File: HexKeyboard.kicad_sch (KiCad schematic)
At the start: 82 parts, among them J1 Conn_02x04_Odd_Even, J2 Conn_01x04, J4 USB_A, J9 Micro_SD_Card, SW1 SW_1, SW10 SW_10, SW11 SW_11, SW12 SW_12, SW13 SW_13, SW14 SW_14, SW15 SW_15, SW16 SW_16, SW17 SW_17, SW18 SW_18, SW19 SW_19, SW2 SW_2, SW20 SW_20, SW21 SW_21, SW22 SW_22, SW23 SW_23, SW24 SW_24, SW25 SW_25, SW3 SW_3, SW4 SW_4, SW5 SW_5, SW6 SW_6, SW7 SW_7, SW8 SW_8, SW9 SW_9, U1 ATmega32U4-AU, U2 AMS1117-3.3, U3 74LVC125, U4 AT24CS64-XHM, U5 MAX7219, Y1 16MHz

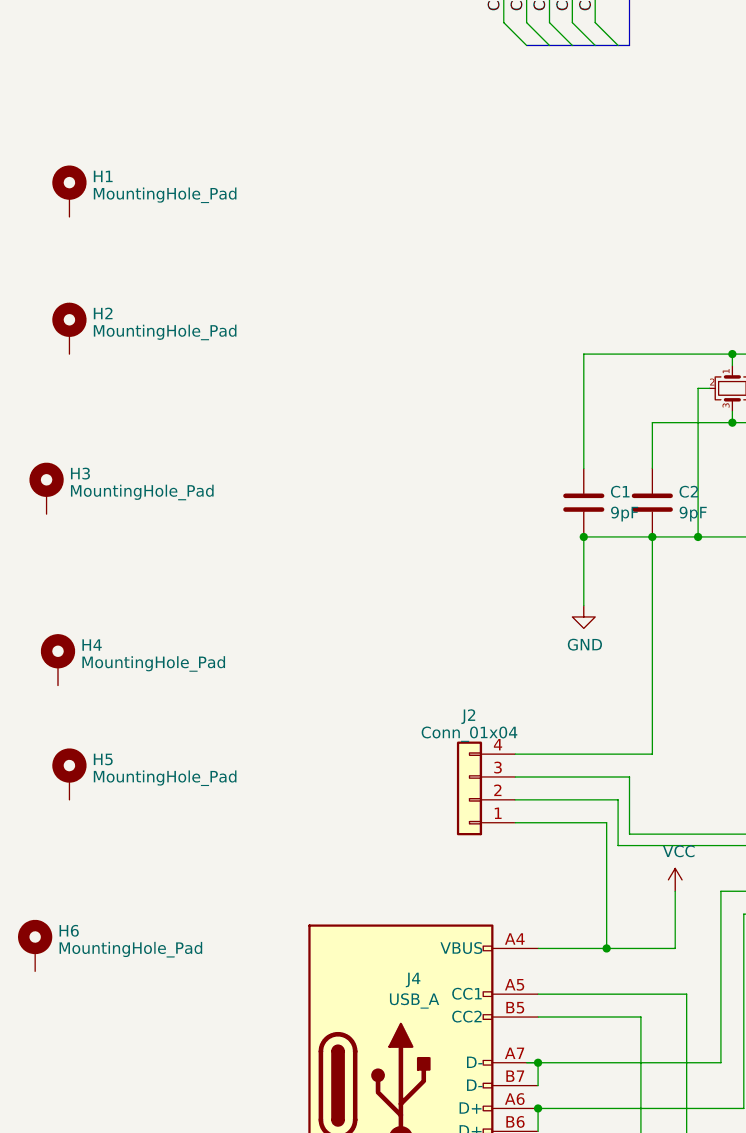
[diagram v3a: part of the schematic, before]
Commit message: Connected mounting holes to Gnd Added filled zone
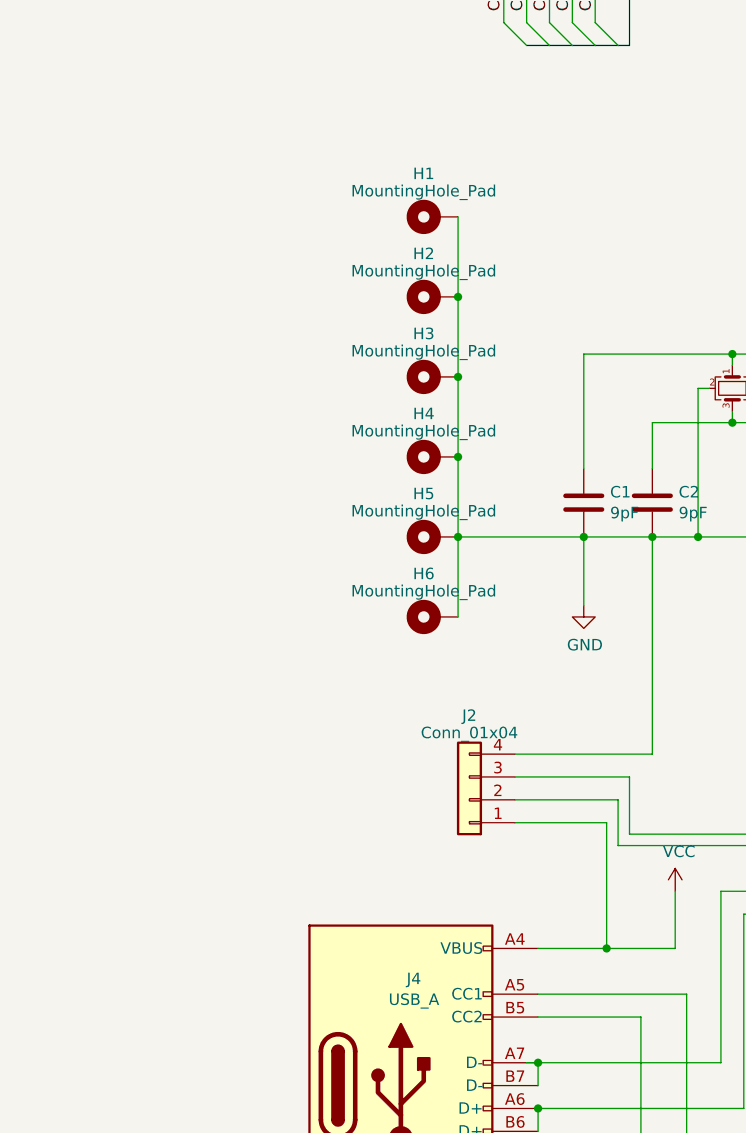
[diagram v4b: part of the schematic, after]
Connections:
- net GND: now also H1.1, H2.1, H3.1, H4.1, H5.1, H6.1
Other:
- moved on the sheet: H1, H2, H3, H4, H5, H6
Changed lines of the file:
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@@
   (junction (at 104.14 66.04) (diameter 0) (color 0 0 0 0)
   )
+  (junction (at 91.44 166.37) (diameter 0) (color 0 0 0 0)
+  )
   (junction (at 121.92 163.83) (diameter 0) (color 0 0 0 0)
   )
   (junction (at 173.99 147.32) (diameter 0) (color 0 0 0 0)
   )
+  (junction (at 91.44 157.48) (diameter 0) (color 0 0 0 0)
+  )
   (junction (at 78.74 68.58) (diameter 0) (color 0 0 0 0)
   )
@@
   (junction (at 78.74 99.06) (diameter 0) (color 0 0 0 0)
   )
+  (junction (at 91.44 175.26) (diameter 0) (color 0 0 0 0)
+  )
   (junction (at 171.45 248.92) (diameter 0) (color 0 0 0 0)
   )
@@
   (junction (at 214.63 115.57) (diameter 0) (color 0 0 0 0)
   )
+  (junction (at 91.44 184.15) (diameter 0) (color 0 0 0 0)
+  )
   (junction (at 132.08 54.61) (diameter 0) (color 0 0 0 0)
   )
@@
     (stroke (width 0) (type default))
   )
+  (wire (pts (xy 91.44 184.15) (xy 91.44 193.04))
+    (stroke (width 0) (type default))
+  )
   (wire (pts (xy 295.91 115.57) (xy 295.91 118.11))
     (stroke (width 0) (type default))
@@
     (stroke (width 0) (type default))
   )
+  (wire (pts (xy 91.44 166.37) (xy 91.44 175.26))
+    (stroke (width 0) (type default))
+  )
   (wire (pts (xy 86.36 111.76) (xy 86.36 115.57))
     (stroke (width 0) (type default))
@@
     (stroke (width 0) (type default))
   )
+  (wire (pts (xy 91.44 148.59) (xy 91.44 157.48))
+    (stroke (width 0) (type default))
+  )
   (wire (pts (xy 226.06 104.14) (xy 226.06 107.95))
     (stroke (width 0) (type default))
@@
     (stroke (width 0) (type default))
   )
+  (wire (pts (xy 91.44 175.26) (xy 91.44 184.15))
+    (stroke (width 0) (type default))
+  )
   (wire (pts (xy 78.74 83.82) (xy 96.52 83.82))
     (stroke (width 0) (type default))
@@
     (stroke (width 0) (type default))
   )
+  (wire (pts (xy 91.44 157.48) (xy 91.44 166.37))
+    (stroke (width 0) (type default))
+  )
   (wire (pts (xy 241.3 158.75) (xy 241.3 166.37))
     (stroke (width 0) (type default))
@@
     (stroke (width 0) (type default))
   )
+  (wire (pts (xy 91.44 184.15) (xy 105.41 184.15))
+    (stroke (width 0) (type default))
+  )
   (wire (pts (xy 60.96 52.07) (xy 60.96 49.53))
     (stroke (width 0) (type default))
@@
     )
   )
-  (symbol (lib_id "Mechanical:MountingHole_Pad") (at 46.99 198.12 0) (unit 1)
+  (symbol (lib_id "Mechanical:MountingHole_Pad") (at 88.9 175.26 90) (unit 1)
     (in_bom yes) (on_board yes) (dnp no) (fields_autoplaced)
-    (property "Reference" "H4" (at 49.53 196.2063 0)
-      (effects (font (size 1.27 1.27)) (justify left))
+    (property "Reference" "H4" (at 87.63 170.4721 90)
+      (effects (font (size 1.27 1.27)))
     )
-    (property "Value" "MountingHole_Pad" (at 49.53 198.1273 0)
-      (effects (font (size 1.27 1.27)) (justify left))
+    (property "Value" "MountingHole_Pad" (at 87.63 172.3931 90)
+      (effects (font (size 1.27 1.27)))
     )
-    (property "Footprint" "MountingHole:MountingHole_3.2mm_M3_Pad_Via" (at 46.99 198.12 0)
+    (property "Footprint" "MountingHole:MountingHole_3.2mm_M3_Pad_Via" (at 88.9 175.26 0)
       (effects (font (size 1.27 1.27)) hide)
     )
-    (property "Datasheet" "~" (at 46.99 198.12 0)
+    (property "Datasheet" "~" (at 88.9 175.26 0)
       (effects (font (size 1.27 1.27)) hide)
     )
@@
     )
   )
-  (symbol (lib_id "Mechanical:MountingHole_Pad") (at 48.26 210.82 0) (unit 1)
+  (symbol (lib_id "Mechanical:MountingHole_Pad") (at 88.9 184.15 90) (unit 1)
     (in_bom yes) (on_board yes) (dnp no) (fields_autoplaced)
-    (property "Reference" "H5" (at 50.8 208.9063 0)
-      (effects (font (size 1.27 1.27)) (justify left))
+    (property "Reference" "H5" (at 87.63 179.3621 90)
+      (effects (font (size 1.27 1.27)))
     )
-    (property "Value" "MountingHole_Pad" (at 50.8 210.8273 0)
-      (effects (font (size 1.27 1.27)) (justify left))
+    (property "Value" "MountingHole_Pad" (at 87.63 181.2831 90)
+      (effects (font (size 1.27 1.27)))
     )
-    (property "Footprint" "MountingHole:MountingHole_3.2mm_M3_Pad_Via" (at 48.26 210.82 0)
+    (property "Footprint" "MountingHole:MountingHole_3.2mm_M3_Pad_Via" (at 88.9 184.15 0)
       (effects (font (size 1.27 1.27)) hide)
     )
-    (property "Datasheet" "~" (at 48.26 210.82 0)
+    (property "Datasheet" "~" (at 88.9 184.15 0)
       (effects (font (size 1.27 1.27)) hide)
     )
@@
     )
   )
-  (symbol (lib_id "Mechanical:MountingHole_Pad") (at 44.45 229.87 0) (unit 1)
+  (symbol (lib_id "Mechanical:MountingHole_Pad") (at 88.9 193.04 90) (unit 1)
     (in_bom yes) (on_board yes) (dnp no) (fields_autoplaced)
-    (property "Reference" "H6" (at 46.99 227.9563 0)
-      (effects (font (size 1.27 1.27)) (justify left))
+    (property "Reference" "H6" (at 87.63 188.2521 90)
+      (effects (font (size 1.27 1.27)))
     )
-    (property "Value" "MountingHole_Pad" (at 46.99 229.8773 0)
-      (effects (font (size 1.27 1.27)) (justify left))
+    (property "Value" "MountingHole_Pad" (at 87.63 190.1731 90)
+      (effects (font (size 1.27 1.27)))
     )
-    (property "Footprint" "MountingHole:MountingHole_3.2mm_M3_Pad_Via" (at 44.45 229.87 0)
+    (property "Footprint" "MountingHole:MountingHole_3.2mm_M3_Pad_Via" (at 88.9 193.04 0)
       (effects (font (size 1.27 1.27)) hide)
     )
-    (property "Datasheet" "~" (at 44.45 229.87 0)
+    (property "Datasheet" "~" (at 88.9 193.04 0)
       (effects (font (size 1.27 1.27)) hide)
     )
@@
     )
   )
-  (symbol (lib_id "Mechanical:MountingHole_Pad") (at 48.26 161.29 0) (unit 1)
+  (symbol (lib_id "Mechanical:MountingHole_Pad") (at 88.9 157.48 90) (unit 1)
     (in_bom yes) (on_board yes) (dnp no) (fields_autoplaced)
-    (property "Reference" "H2" (at 50.8 159.3763 0)
-      (effects (font (size 1.27 1.27)) (justify left))
+    (property "Reference" "H2" (at 87.63 152.6921 90)
+      (effects (font (size 1.27 1.27)))
     )
-    (property "Value" "MountingHole_Pad" (at 50.8 161.2973 0)
-      (effects (font (size 1.27 1.27)) (justify left))
+    (property "Value" "MountingHole_Pad" (at 87.63 154.6131 90)
+      (effects (font (size 1.27 1.27)))
     )
-    (property "Footprint" "MountingHole:MountingHole_3.2mm_M3_Pad_Via" (at 48.26 161.29 0)
+    (property "Footprint" "MountingHole:MountingHole_3.2mm_M3_Pad_Via" (at 88.9 157.48 0)
       (effects (font (size 1.27 1.27)) hide)
     )
-    (property "Datasheet" "~" (at 48.26 161.29 0)
+    (property "Datasheet" "~" (at 88.9 157.48 0)
       (effects (font (size 1.27 1.27)) hide)
     )
@@
     )
   )
-  (symbol (lib_id "Mechanical:MountingHole_Pad") (at 45.72 179.07 0) (unit 1)
+  (symbol (lib_id "Mechanical:MountingHole_Pad") (at 88.9 166.37 90) (unit 1)
     (in_bom yes) (on_board yes) (dnp no) (fields_autoplaced)
-    (property "Reference" "H3" (at 48.26 177.1563 0)
-      (effects (font (size 1.27 1.27)) (justify left))
+    (property "Reference" "H3" (at 87.63 161.5821 90)
+      (effects (font (size 1.27 1.27)))
     )
-    (property "Value" "MountingHole_Pad" (at 48.26 179.0773 0)
-      (effects (font (size 1.27 1.27)) (justify left))
+    (property "Value" "MountingHole_Pad" (at 87.63 163.5031 90)
+      (effects (font (size 1.27 1.27)))
     )
-    (property "Footprint" "MountingHole:MountingHole_3.2mm_M3_Pad_Via" (at 45.72 179.07 0)
+    (property "Footprint" "MountingHole:MountingHole_3.2mm_M3_Pad_Via" (at 88.9 166.37 0)
       (effects (font (size 1.27 1.27)) hide)
     )
-    (property "Datasheet" "~" (at 45.72 179.07 0)
+    (property "Datasheet" "~" (at 88.9 166.37 0)
       (effects (font (size 1.27 1.27)) hide)
     )
@@
     )
   )
-  (symbol (lib_id "Mechanical:MountingHole_Pad") (at 48.26 146.05 0) (unit 1)
+  (symbol (lib_id "Mechanical:MountingHole_Pad") (at 88.9 148.59 90) (unit 1)
     (in_bom yes) (on_board yes) (dnp no) (fields_autoplaced)
-    (property "Reference" "H1" (at 50.8 144.1363 0)
-      (effects (font (size 1.27 1.27)) (justify left))
+    (property "Reference" "H1" (at 87.63 143.8021 90)
+      (effects (font (size 1.27 1.27)))
     )
-    (property "Value" "MountingHole_Pad" (at 50.8 146.0573 0)
-      (effects (font (size 1.27 1.27)) (justify left))
+    (property "Value" "MountingHole_Pad" (at 87.63 145.7231 90)
+      (effects (font (size 1.27 1.27)))
     )
-    (property "Footprint" "MountingHole:MountingHole_3.2mm_M3_Pad_Via" (at 48.26 146.05 0)
+    (property "Footprint" "MountingHole:MountingHole_3.2mm_M3_Pad_Via" (at 88.9 148.59 0)
       (effects (font (size 1.27 1.27)) hide)
     )
-    (property "Datasheet" "~" (at 48.26 146.05 0)
+    (property "Datasheet" "~" (at 88.9 148.59 0)
       (effects (font (size 1.27 1.27)) hide)
     )
